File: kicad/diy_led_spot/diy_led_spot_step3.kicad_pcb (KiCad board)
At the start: 2 copper layers, 50.5 x 47.5 mm, 33 parts, among them Q1 AO3400A_C347475, U1 DCDCStepDown, U2 PT4115, U3 ESP32-C3_SUPERMINI_SMD, U4 MT3608, U5 110kΩ

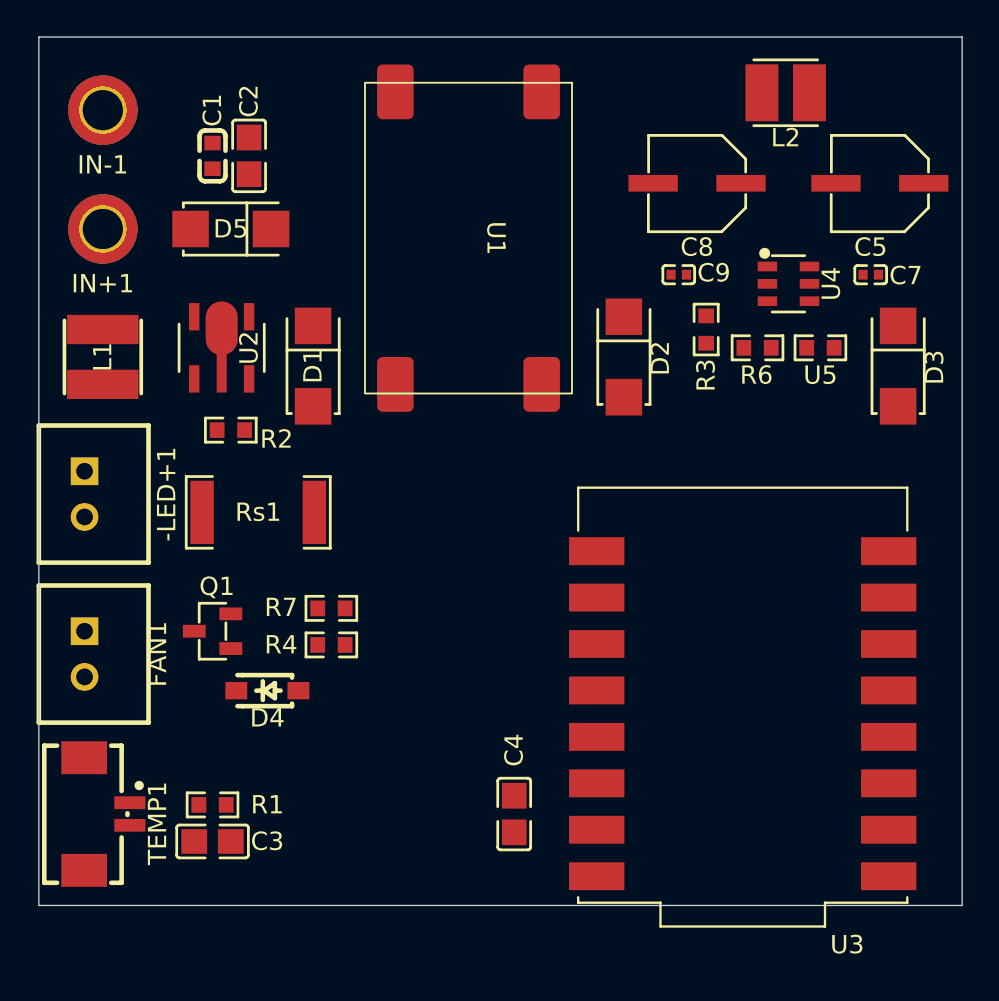
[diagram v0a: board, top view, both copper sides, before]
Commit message: kicad: save current PCB/schematic state including routed and step3 variants
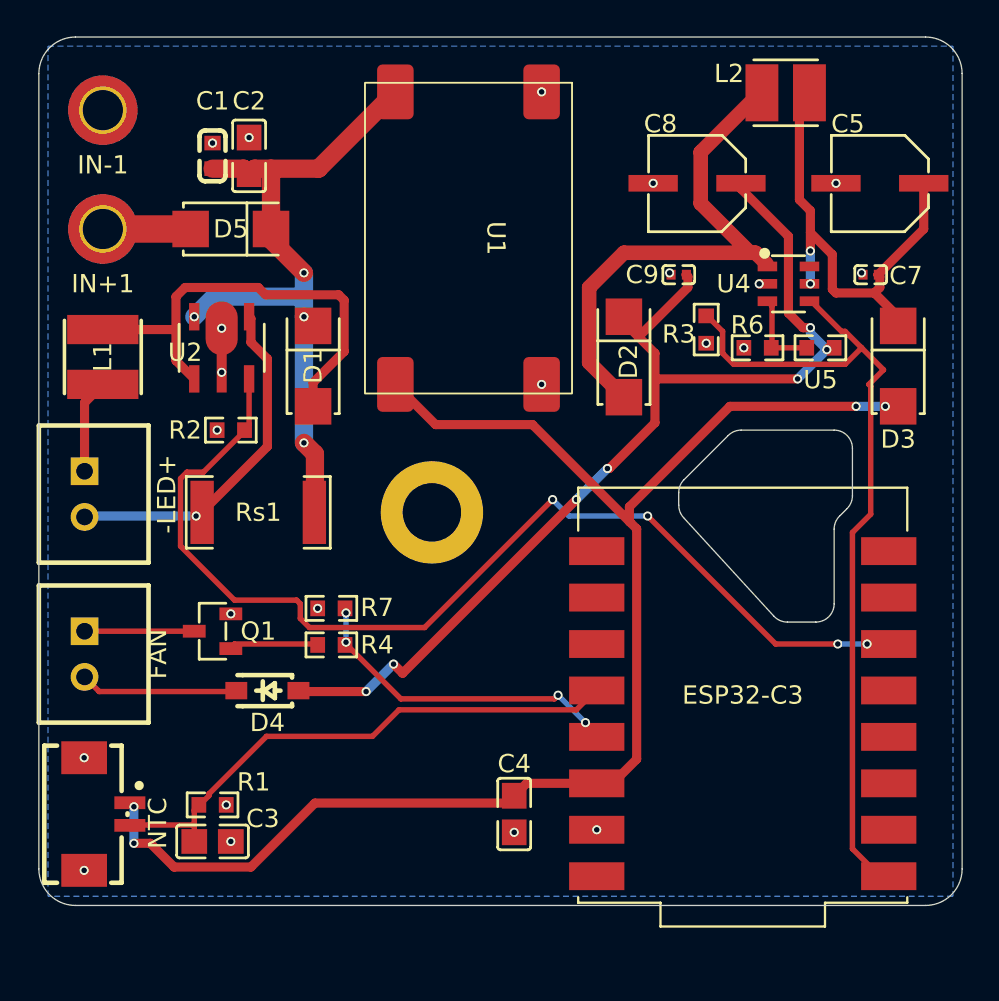
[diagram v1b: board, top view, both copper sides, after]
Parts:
- added REF**: MountingHole_3.2mm_M3_DIN965_Pad, MountingHole:MountingHole_3.2mm_M3_DIN965_Pad, F.Cu at (133.5, 86.0)
- renumbered -LED+1 to -LED+, U3 to ESP32-C3, FAN1 to FAN, TEMP1 to NTC
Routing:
- net +3.3V: track 0.00 -> 79.7 mm, vias 0 -> 4
- net +5V: track 0.00 -> 59.0 mm, vias 0 -> 7
- net PWM: track 0.00 -> 58.6 mm, vias 0 -> 4
- net 5VEN: track 0.00 -> 46.1 mm
- net +24V: track 0.00 -> 39.0 mm, vias 0 -> 4
- net NTC: track 0.00 -> 30.2 mm
- net Net-(D2-A): track 0.00 -> 28.9 mm
- net Net-(D3-K): track 0.00 -> 26.7 mm, vias 0 -> 2
- net Net-(D1-A): track 0.00 -> 25.1 mm
- net LED+: track 0.00 -> 19.2 mm, vias 0 -> 1
- net FANPWM: track 0.00 -> 18.3 mm, vias 0 -> 4
- net Net-(D4-C): track 0.00 -> 8.68 mm
- net Net-(Q1-D): track 0.00 -> 6.00 mm
- net LED-: track 0.00 -> 5.26 mm
- net Net-(Q1-G): track 0.00 -> 4.90 mm
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- added copper zone on B.Cu, net GND
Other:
- outline, holes or cut-outs redrawn

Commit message: kicad: save current PCB/schematic state
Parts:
- removed NTC: MX1.25-2P, easyeda2kicad:CONN-SMD_2P-P1.25_XUNPU_WAFER-MX1.25-2PWB
- added G***: LOGO, diy_led_spot.preety:diy_led_spot-back, B.Cu at (138.0, 83.8)
- added REF**: MountingHole_2.2mm_M2_ISO7380_Pad, MountingHole:MountingHole_2.2mm_M2_ISO7380_Pad, F.Cu at (144.5, 62.5)
- added REF**: MountingHole_2.2mm_M2_ISO7380_Pad, MountingHole:MountingHole_2.2mm_M2_ISO7380_Pad, F.Cu at (160.0, 62.5)
- added TEMP1: BX-XH2.54-2PZZ, easyeda2kicad:CONN-TH_2P-P2.50_BX-XH2.54-2PZZ, F.Cu at (114.5, 102.5)
- D4: value 1N4148W-7-F -> SS36; footprint easyeda2kicad:SOD-123_L2.7-W1.6-LS3.7-RD-1 -> easyeda2kicad:SMA_L4.3-W2.6-LS5.2-RD
- moved REF** 17.8 mm to (132.8, 103.8)
- moved R1 3.82 mm to (123.5, 105.2)
- moved D4 2.35 mm to (126.8, 96.2)
- moved C3 2.24 mm to (123.5, 103.0)
- moved IN+1 0.50 mm to (115.5, 71.0)
- renumbered -LED+ to -LED+1, FAN to FAN1, ESP32-C3 to U3
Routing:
- net NTC: track 30.2 -> 43.7 mm
- net +3.3V: track 79.7 -> 90.5 mm, vias 4 -> 8
- net Net-(D2-A): track 28.9 -> 21.9 mm
- net +24V: track 39.0 -> 44.9 mm, vias 4 -> 3
- net 5VEN: track 46.1 -> 41.7 mm, vias 0 -> 2
- net +5V: track 59.0 -> 55.5 mm, vias 7 -> 2
- net PWM: track 58.6 -> 56.1 mm
- net Net-(D4-K): track 8.68 -> 10.6 mm
- net FANPWM: track 18.3 -> 18.0 mm, vias 4 -> 2
- net GND: vias 22 -> 21
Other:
- outline, holes or cut-outs redrawn

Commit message: kicad: save current PCB/schematic state
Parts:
- moved G*** 2.15 mm to (139.2, 85.5)
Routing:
- net PWM: track 56.1 -> 54.4 mm
